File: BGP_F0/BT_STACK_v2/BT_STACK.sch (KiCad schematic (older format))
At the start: 19 parts, among them P1 CONN_01X05, P3 CONN_01X04, U1 MC33178

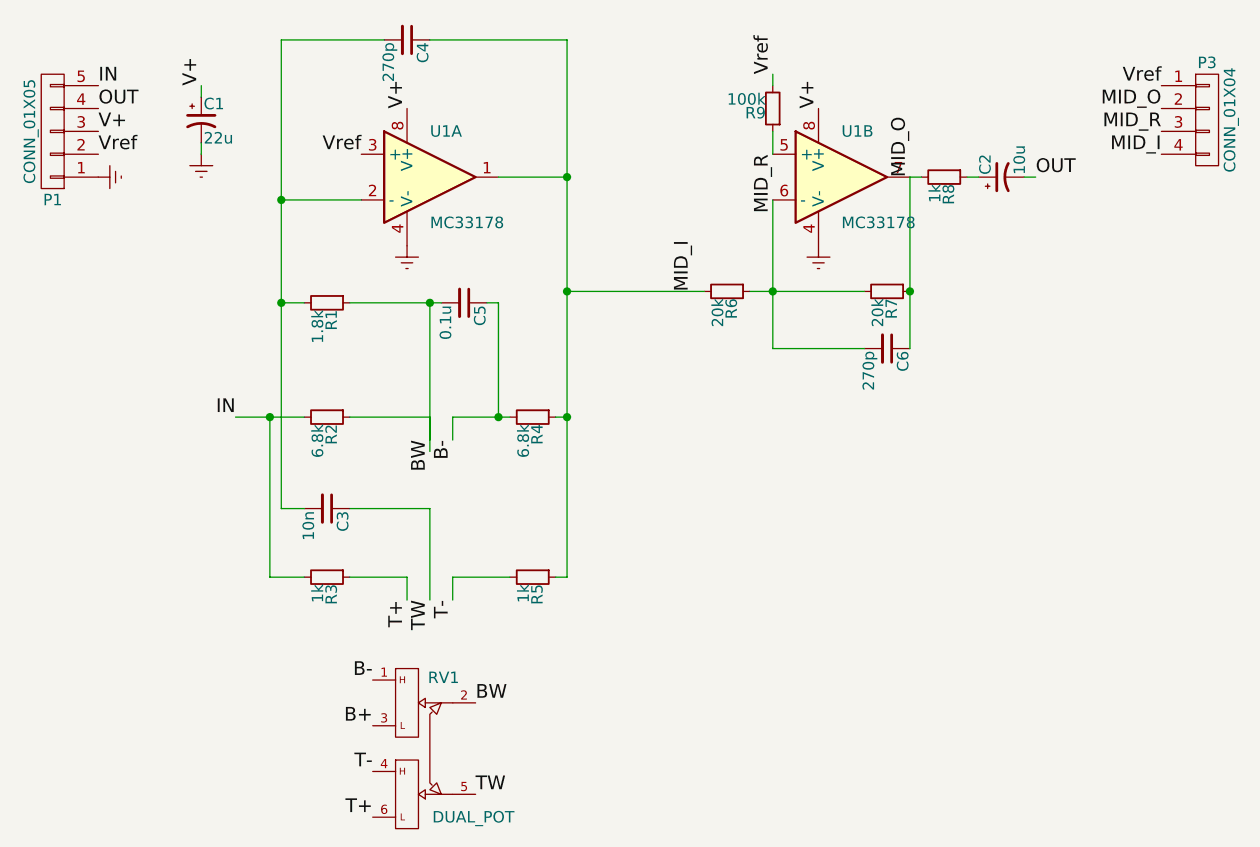
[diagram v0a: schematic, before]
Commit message: F0 - Boost only - boost/cut bypass
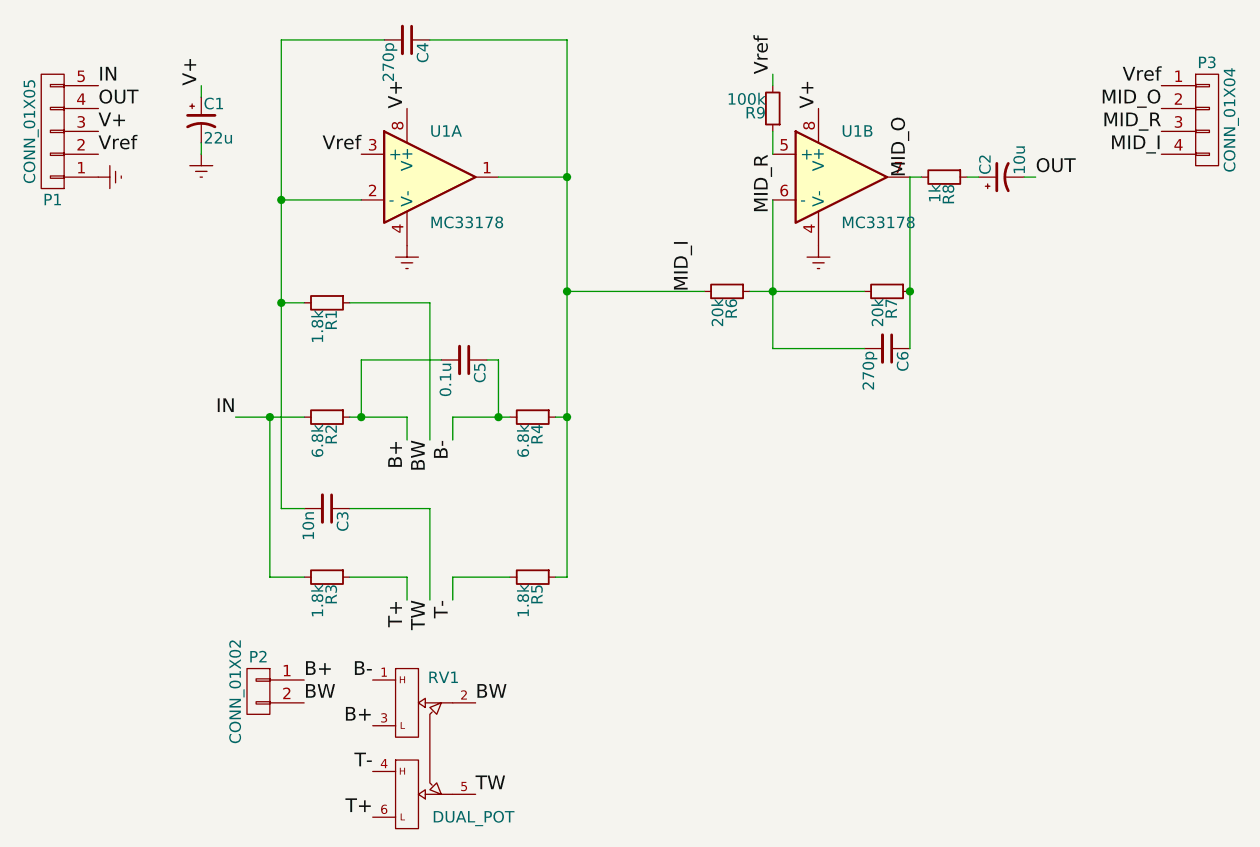
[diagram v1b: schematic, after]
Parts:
- added P2: CONN_01X02, Pin_Headers:Pin_Header_Straight_1x02, symbol CONN_01X02
- R3, R5: value 1k -> 1.8k
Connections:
- net B+: now also C5.2, R2.1, P2.1 (P1)
- net BW: now also P2.2 (P2); no longer C5.2, R2.1
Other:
- moved on the sheet: C5
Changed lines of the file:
@@
 L C_Small C5
 U 1 1 5A288B14
-P 5550 3250
-F 0 "C5" H 5560 3320 50  0000 L CNN
-F 1 "0.1u" H 5560 3170 50  0000 L CNN
-F 2 "Capacitors_SMD:C_0805_HandSoldering" H 5550 3250 50  0001 C CNN
-F 3 "" H 5550 3250 50  0000 C CNN
-	1    5550 3250
+P 5550 3500
+F 0 "C5" H 5560 3570 50  0000 L CNN
+F 1 "0.1u" H 5560 3420 50  0000 L CNN
+F 2 "Capacitors_SMD:C_0805_HandSoldering" H 5550 3500 50  0001 C CNN
+F 3 "" H 5550 3500 50  0000 C CNN
+	1    5550 3500
 	0    1    1    0
 $EndComp
@@
 P 4950 4450
 F 0 "R3" H 4980 4470 50  0000 L CNN
-F 1 "1k" H 4980 4410 50  0000 L CNN
+F 1 "1.8k" H 4980 4410 50  0000 L CNN
 F 2 "Resistors_SMD:R_0603_HandSoldering" H 4950 4450 50  0001 C CNN
 F 3 "" H 4950 4450 50  0000 C CNN
@@
 P 5850 4450
 F 0 "R5" H 5880 4470 50  0000 L CNN
-F 1 "1k" H 5880 4410 50  0000 L CNN
+F 1 "1.8k" H 5880 4410 50  0000 L CNN
 F 2 "Resistors_SMD:R_0603_HandSoldering" H 5850 4450 50  0001 C CNN
 F 3 "" H 5850 4450 50  0000 C CNN
@@
 	5700 2700 6000 2700
 Wire Wire Line
-	5050 3750 5400 3750
-Wire Wire Line
 	5500 3850 5500 3750
 Wire Wire Line
 	5500 3750 5750 3750
-Wire Wire Line
-	5050 3250 5450 3250
 Wire Wire Line
 	4750 3250 4850 3250
 Connection ~ 4750 2800
 Connection ~ 6000 2700
-Wire Wire Line
-	5400 3850 5400 3250
 Wire Wire Line
 	6000 2100 6000 4450
@@
 Wire Wire Line
 	6900 2250 6900 2300
-Wire Wire Line
-	5400 3750 5400 3900
-Wire Wire Line
-	5700 3750 5700 3250
-Wire Wire Line
-	5700 3250 5650 3250
 Connection ~ 5700 3750
-Connection ~ 5400 3250
+Wire Wire Line
+	5400 3250 5400 3850
+Wire Wire Line
+	5700 3750 5700 3500
+Wire Wire Line
+	5700 3500 5650 3500
+Wire Wire Line
+	5050 3750 5300 3750
+Wire Wire Line
+	5300 3750 5300 3850
+Wire Wire Line
+	5400 3250 5050 3250
+Wire Wire Line
+	5100 3750 5100 3500
+Wire Wire Line
+	5100 3500 5450 3500
+Connection ~ 5100 3750
+Text Label 5300 3850 3    60   ~ 0
+B+
+$Comp
+L CONN_01X02 P2
+U 1 1 5AF39016
+P 4650 4950
+F 0 "P2" H 4650 5100 50  0000 C CNN
+F 1 "CONN_01X02" V 4750 4950 50  0000 C CNN
+F 2 "Pin_Headers:Pin_Header_Straight_1x02" H 4650 4950 50  0001 C CNN
+F 3 "" H 4650 4950 50  0000 C CNN
+	1    4650 4950
+	-1   0    0    -1
+$EndComp
+Text Label 4850 4900 0    60   ~ 0
+B+
+Text Label 4850 5000 0    60   ~ 0
+BW
 $EndSCHEMATC

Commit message: Slight changes
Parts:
- C4, C6: footprint Capacitors_SMD:C_0603 -> Capacitors_SMD:C_0603_HandSoldering
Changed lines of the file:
@@
 F 0 "C4" H 5310 2170 50  0000 L CNN
 F 1 "270p" H 5310 2020 50  0000 L CNN
-F 2 "Capacitors_SMD:C_0603" H 5300 2100 50  0001 C CNN
+F 2 "Capacitors_SMD:C_0603_HandSoldering" H 5300 2100 50  0001 C CNN
 F 3 "" H 5300 2100 50  0000 C CNN
 	1    5300 2100
@@
 F 0 "C6" H 7410 3520 50  0000 L CNN
 F 1 "270p" H 7410 3370 50  0000 L CNN
-F 2 "Capacitors_SMD:C_0603" H 7400 3450 50  0001 C CNN
+F 2 "Capacitors_SMD:C_0603_HandSoldering" H 7400 3450 50  0001 C CNN
 F 3 "" H 7400 3450 50  0000 C CNN
 	1    7400 3450

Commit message: F0 BT Layout
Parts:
- P2: footprint Pin_Headers:Pin_Header_Straight_1x02 -> Pin_Headers:Pin_Header_Straight_1x02_Pitch2.54mm
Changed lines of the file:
@@
 F 0 "P2" H 4650 5100 50  0000 C CNN
 F 1 "CONN_01X02" V 4750 4950 50  0000 C CNN
-F 2 "Pin_Headers:Pin_Header_Straight_1x02" H 4650 4950 50  0001 C CNN
+F 2 "Pin_Headers:Pin_Header_Straight_1x02_Pitch2.54mm" H 4650 4950 50  0001 C CNN
 F 3 "" H 4650 4950 50  0000 C CNN
 	1    4650 4950
